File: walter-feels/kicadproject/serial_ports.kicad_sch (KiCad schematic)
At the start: 23 parts, among them Q4 NX7002AK,215, U2 MAX3221, U3 DS9503P+, U4 THVD1450D, U5 SN74LVC1G125DBVR, U6 SN74LVC1G125DBVR

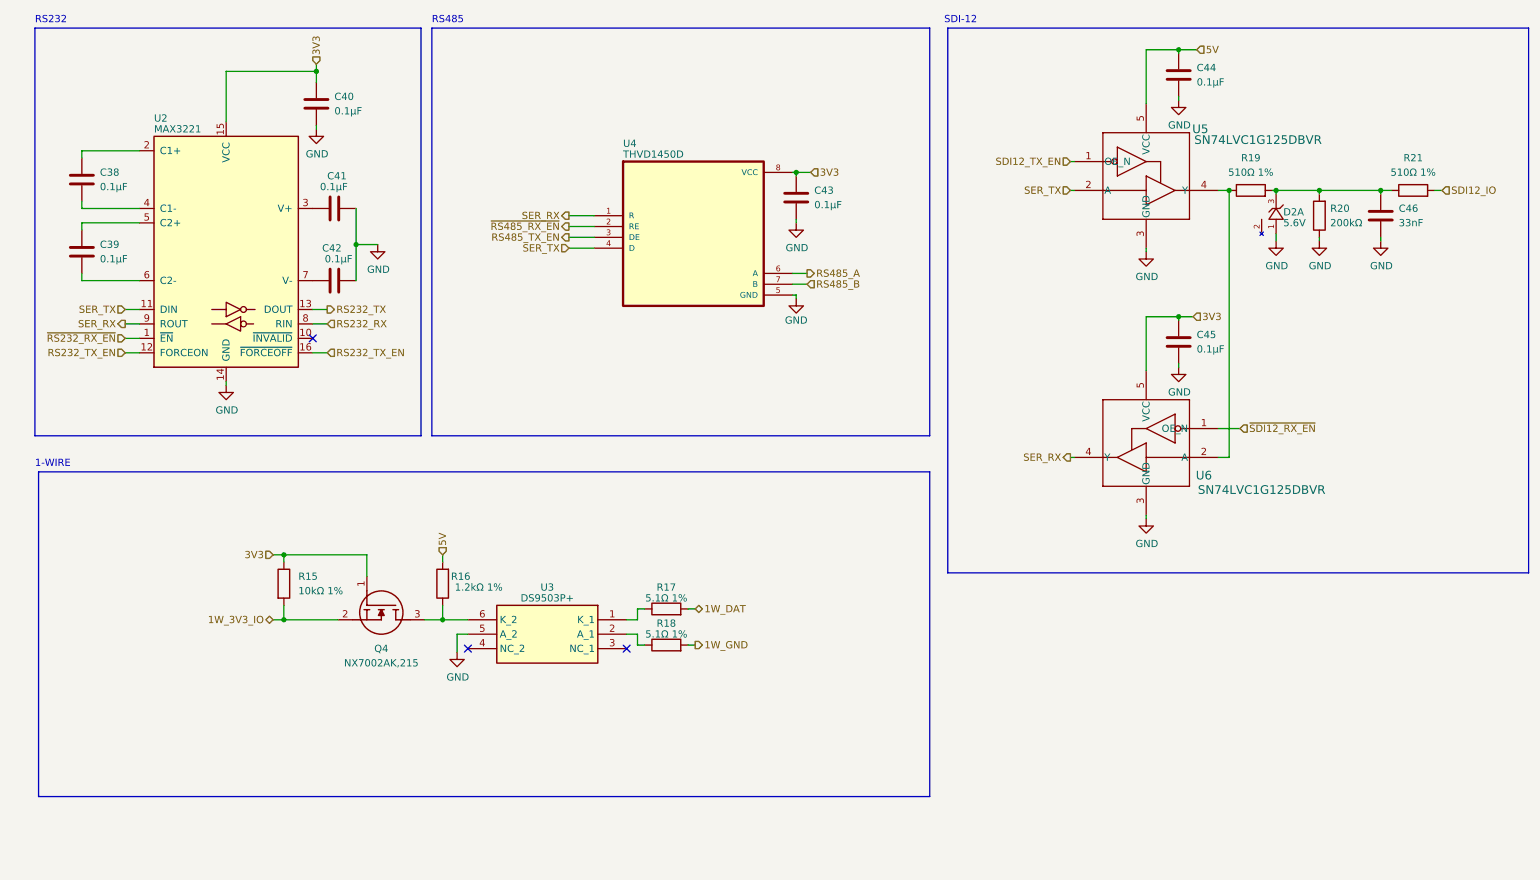
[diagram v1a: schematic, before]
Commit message: Updated Walter Feels to V2.3
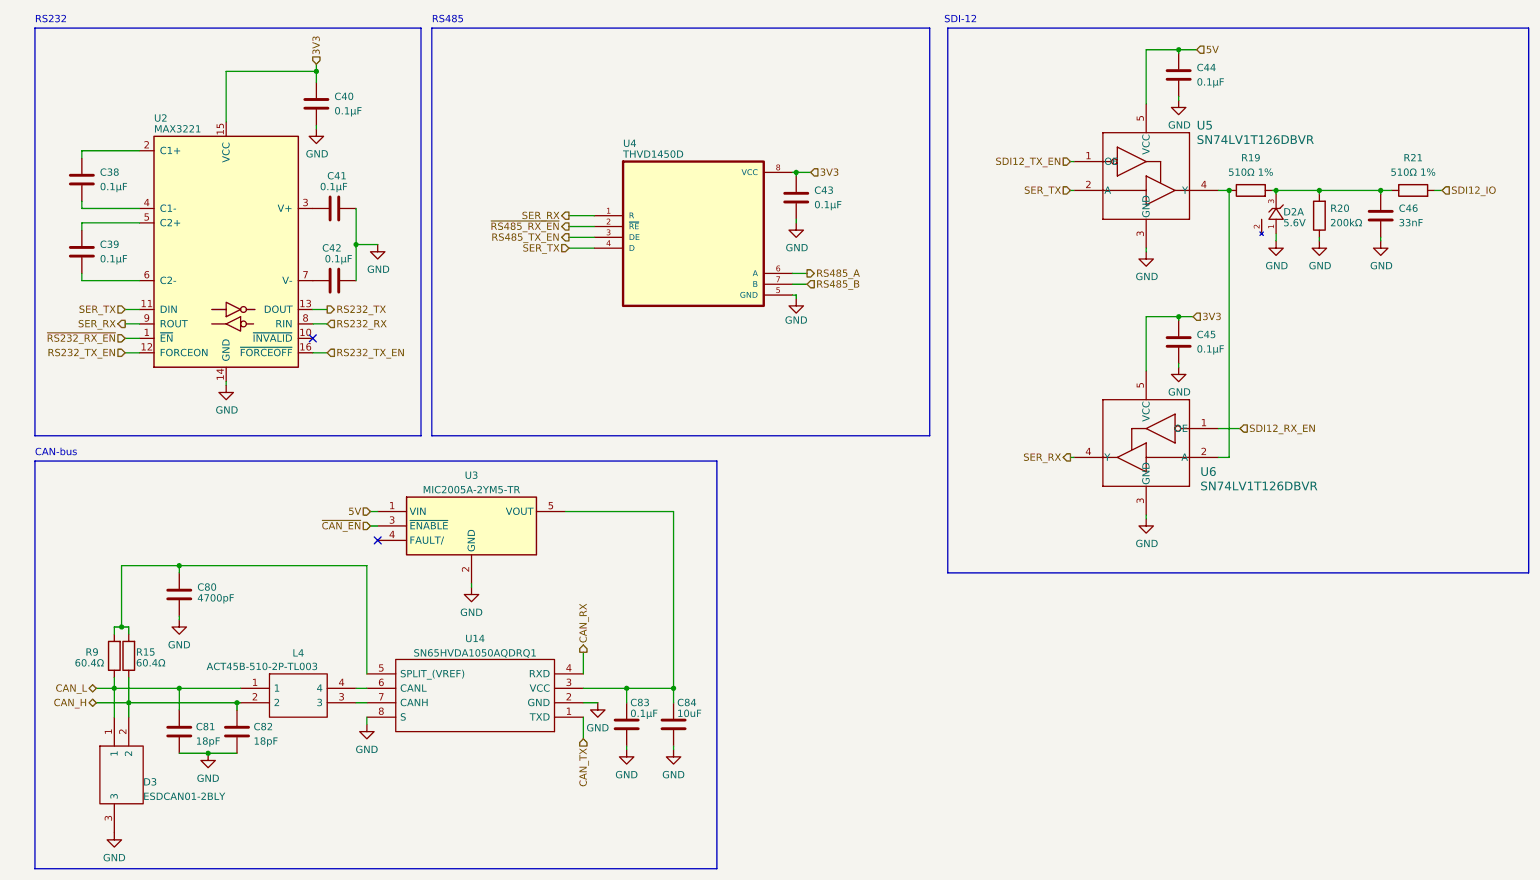
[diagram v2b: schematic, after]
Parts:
- removed Q4: NX7002AK,215, NX7002AK:TL431CDBZR215, symbol NX7002AK:NX7002AK,215
- removed R16: 1.2kΩ 1%, Resistor_SMD:R_0603_1608Metric, symbol Device:R
- removed R17, R18: 5.1Ω 1%, Resistor_SMD:R_0603_1608Metric, symbol Device:R
- removed U3: DS9503P+, DS9503P+:DS2505PTR, symbol DS9503P+:DS9503P+
- added C80: 4700pF, Capacitor_SMD:C_0603_1608Metric, symbol Device:C
- added C81, C82: 18pF, Capacitor_SMD:C_0603_1608Metric, symbol Device:C
- added C83: 0.1µF, Capacitor_SMD:C_0603_1608Metric, symbol Device:C
- added C84: 10uF, Capacitor_SMD:C_0603_1608Metric, symbol Device:C
- added D3: ESDCAN01-2BLY, ESDCAN01-2BLY:SOT95P255X150-3N, symbol ESDCAN01-2BLY:ESDCAN01-2BLY
- added L4: ACT45B-510-2P-TL003, ACT45B-510-2P-TL003:ACT45B1012PTL003, symbol ACT45B-510-2P-TL003:ACT45B-510-2P-TL003
- added R9: 60.4Ω, Resistor_SMD:R_0603_1608Metric, symbol Device:R
- added U14: SN65HVDA1050AQDRQ1, SN65HVDA1050AQDRQ1:SOIC127P600X175-8N, symbol SN65HVDA1050AQDRQ1:SN65HVDA1050AQDRQ1
- added U3: MIC2005A-2YM5-TR, MIC2005A-2YM5-TR:MIC2005A-2YM5, symbol MIC2005A-2YM5-TR:MIC2005A-2YM5-TR
- R15: value 10kΩ 1% -> 60.4Ω; JLCPCB C25804 -> C2933247
- U5, U6: value SN74LVC1G125DBVR -> SN74LV1T126DBVR; JLCPCB C23654 -> C2440228
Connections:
- net 3V3: no longer R15.1
- net 5V: now also U3.1 (VIN)
- net GND: now also C80.2, C81.2, C82.2, C83.2, C84.2, D3.3, U14.2 (GND), U14.8 (S), U3.2 (GND)
- net 1W_3V3_IO: no longer names the net of R15.2
- net 1W_3V3_IO: now also C80.1, R9.2, U14.5 (SPLIT_(VREF))
- net ~{SDI12_RX_EN} renamed SDI12_RX_EN
- new net: C83.1, C84.1, U14.3 (VCC), U3.5 (VOUT)
- new net: L4.3, U14.7 (CANH)
- new net: L4.4, U14.6 (CANL)
- new net CAN_H: C82.1, D3.2, L4.2, R15.1
- new net CAN_L: C81.1, D3.1, L4.1, R9.1
- new net CAN_RX: U14.4 (RXD)
- new net CAN_TX: U14.1 (TXD)
- new net ~{CAN_EN}: U3.3 (~{ENABLE})
- no-connect marks 3 -> 2
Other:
- note added: "CAN-bus"
- note removed: "1-WIRE"

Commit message: Updated Walter Feels project to version 2.6
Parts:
- C84: value 10uF -> 4.7μF; JLCPCB C19702 -> C19666
- U5, U6: JLCPCB C2440228 -> C23654
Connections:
- net GND: now also C84.1; no longer C84.2
- net at C83.1, U14.3 (VCC), U3.5 (VOUT): now also C84.2; no longer C84.1
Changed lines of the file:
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@@
   (title_block
     (title "Walter Feels")
-    (date "2025-02-12")
-    (rev "2.4")
+    (date "2026-01-13")
+    (rev "2.6")
     (company "DPTechnics BV")
     (comment 1 "Checked by: Jonas Maes")
@@
       (effects (font (size 1.27 1.27) italic) hide)
     )
-    (property "Datasheet" "SN74LV1T126DBVR" (id 3) (at 238.76 31.75 0)
+    (property "Datasheet" "SN74LVC1G125DBVR" (id 3) (at 238.76 31.75 0)
       (effects (font (size 1.27 1.27) italic) hide)
     )
-    (property "JLCPCB" "C2440228" (id 4) (at 232.41 29.845 0)
+    (property "JLCPCB" "C23654" (id 4) (at 232.41 29.845 0)
       (effects (font (size 1.27 1.27)) hide)
     )
@@
     )
     (property "PAGE" "" (id 5) (at 27.305 47.625 0)
-      (effects (font (size 1.27 1.27)) hide)
-    )
-    (pin "1")
-    (pin "2")
-  )
-  (symbol (lib_id "Device:C") (at 131.445 143.51 0) (unit 1)
-    (in_bom yes) (on_board yes)
-    (property "Reference" "C84" (id 0) (at 132.08 139.7 0)
-      (effects (font (size 1.27 1.27)) (justify left))
-    )
-    (property "Value" "10uF" (id 1) (at 132.08 141.605 0)
-      (effects (font (size 1.27 1.27)) (justify left))
-    )
-    (property "Footprint" "Capacitor_SMD:C_0603_1608Metric" (id 2) (at 132.4102 147.32 0)
-      (effects (font (size 1.27 1.27)) hide)
-    )
-    (property "Datasheet" "~" (id 3) (at 131.445 143.51 0)
-      (effects (font (size 1.27 1.27)) hide)
-    )
-    (property "JLCPCB" "C19702" (id 4) (at 131.445 143.51 0)
       (effects (font (size 1.27 1.27)) hide)
     )
@@
     (pin "3")
   )
+  (symbol (lib_id "Device:C") (at 131.445 143.51 180) (unit 1)
+    (in_bom yes) (on_board yes)
+    (property "Reference" "C84" (id 0) (at 132.08 139.7 0)
+      (effects (font (size 1.27 1.27)) (justify right))
+    )
+    (property "Value" "4.7μF" (id 1) (at 132.08 141.605 0)
+      (effects (font (size 1.27 1.27)) (justify right))
+    )
+    (property "Footprint" "Capacitor_SMD:C_0603_1608Metric" (id 2) (at 130.4798 139.7 0)
+      (effects (font (size 1.27 1.27)) hide)
+    )
+    (property "Datasheet" "~" (id 3) (at 131.445 143.51 0)
+      (effects (font (size 1.27 1.27)) hide)
+    )
+    (property "JLCPCB" "C19666" (id 4) (at 131.445 143.51 0)
+      (effects (font (size 1.27 1.27)) hide)
+    )
+    (property "PAGE" "" (id 5) (at 131.445 143.51 0)
+      (effects (font (size 1.27 1.27)) hide)
+    )
+    (pin "1")
+    (pin "2")
+  )
   (symbol (lib_id "Device:C") (at 220.345 76.2 0) (unit 1)
     (in_bom yes) (on_board yes)
@@
       (effects (font (size 1.27 1.27) italic) hide)
     )
-    (property "Datasheet" "SN74LV1T126DBVR" (id 3) (at 238.76 78.74 0)
+    (property "Datasheet" "SN74LVC1G125DBVR" (id 3) (at 238.76 78.74 0)
       (effects (font (size 1.27 1.27) italic) hide)
     )
-    (property "JLCPCB" "C2440228" (id 4) (at 232.41 76.835 0)
-      (effects (font (size 1.27 1.27)) hide)
-    )
+    (property "JLCPCB" "C23654" (id 4) (at 232.41 76.835 0)
+      (effects (font (size 1.27 1.27)) hide)
+    )
